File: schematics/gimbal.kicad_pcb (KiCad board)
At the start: 2 copper layers, 39.4 x 50.8 mm, 7 parts, among them M1 Motor_Servo, M2 Motor_Servo, U1 LM7805_TO220, U2 GY-521, U3 Joystick

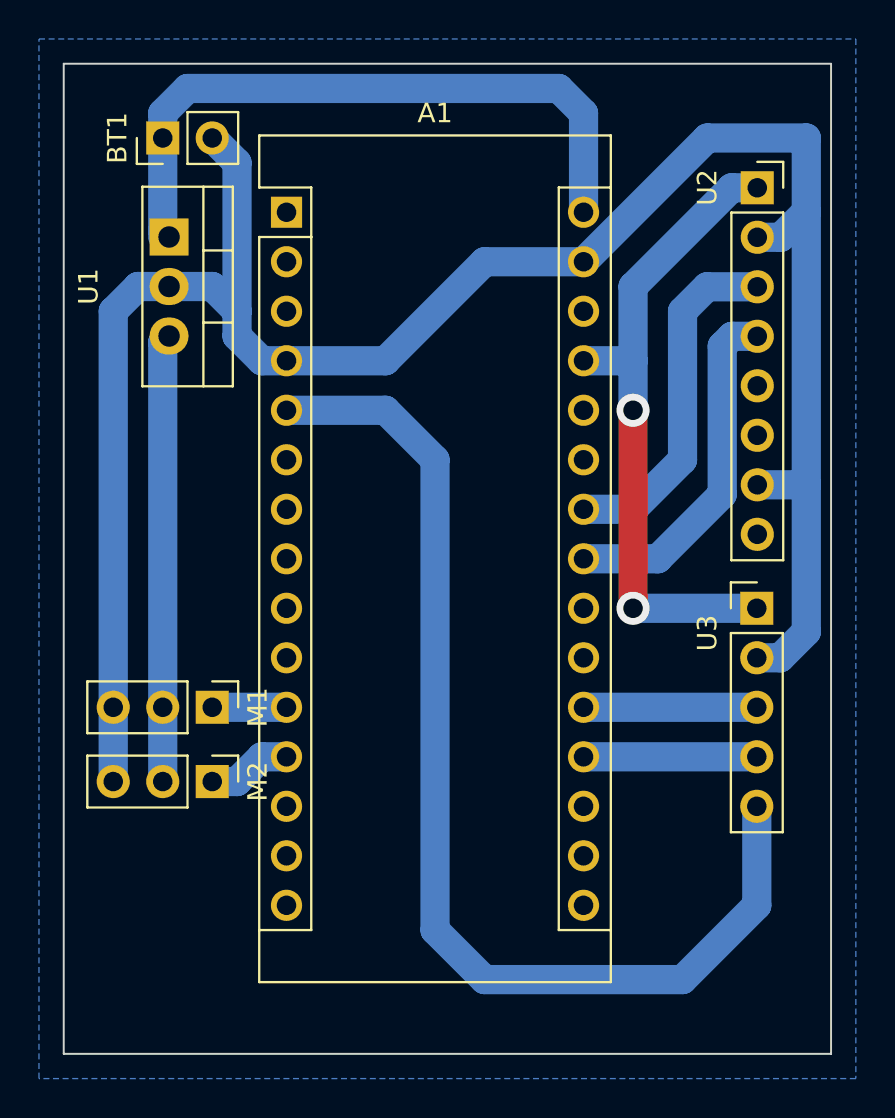
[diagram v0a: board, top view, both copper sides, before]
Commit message: logo + name + smaller board
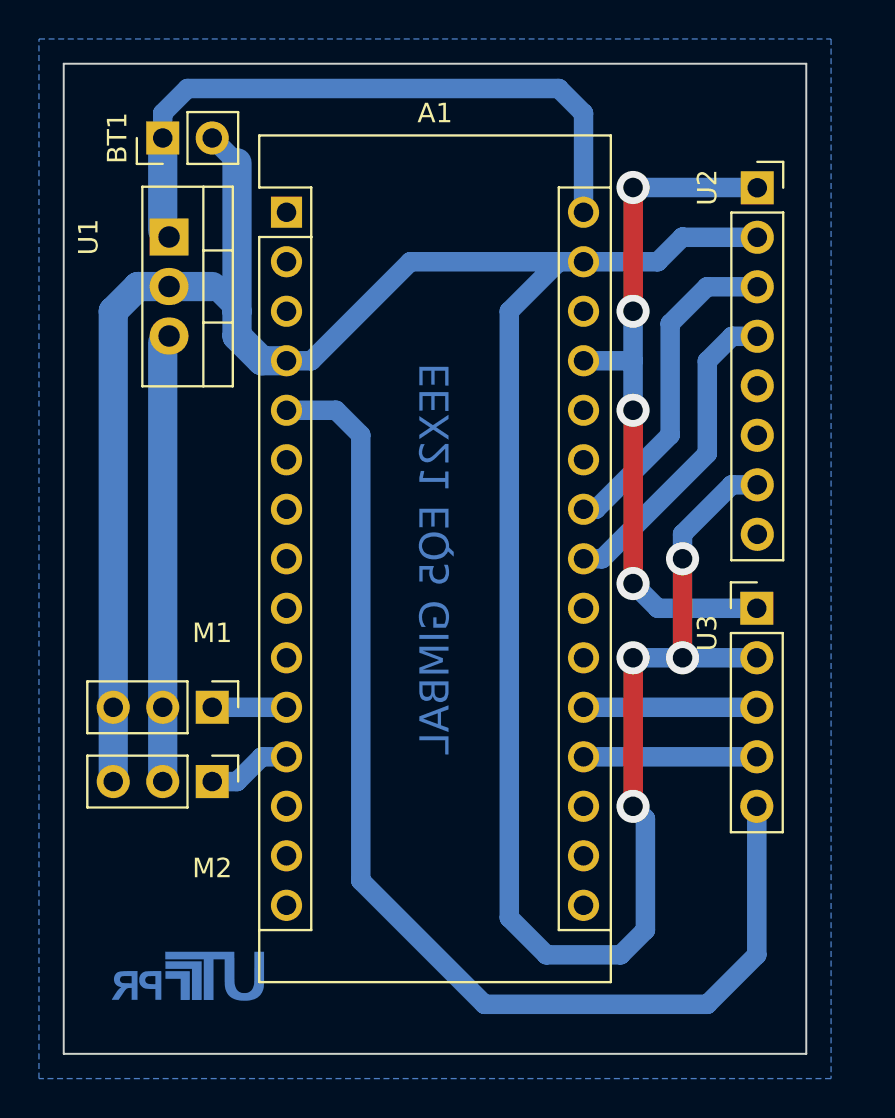
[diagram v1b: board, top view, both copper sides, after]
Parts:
- added Logo: LOGO, images:utfpr, B.Cu at (137.2, 111.8)
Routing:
- net Earth: track 110.7 -> 146.9 mm, vias 0 -> 4
- net +5V: track 33.9 -> 36.1 mm, vias 2 -> 4
- net Net-(A1-Pad5): track 57.0 -> 58.8 mm
- net Net-(A1-Pad23): track 18.1 -> 16.4 mm
- net Net-(A1-Pad24): track 18.1 -> 17.0 mm
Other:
- board size 39.4 x 50.8 mm -> 38.1 x 50.8 mm
- board text added: "EEX21 EQ5 GIMBAL"
